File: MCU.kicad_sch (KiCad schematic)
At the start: 3 parts, among them J2 Micro_SD_Card, U3 STM32H503KBUx, U7 47L16

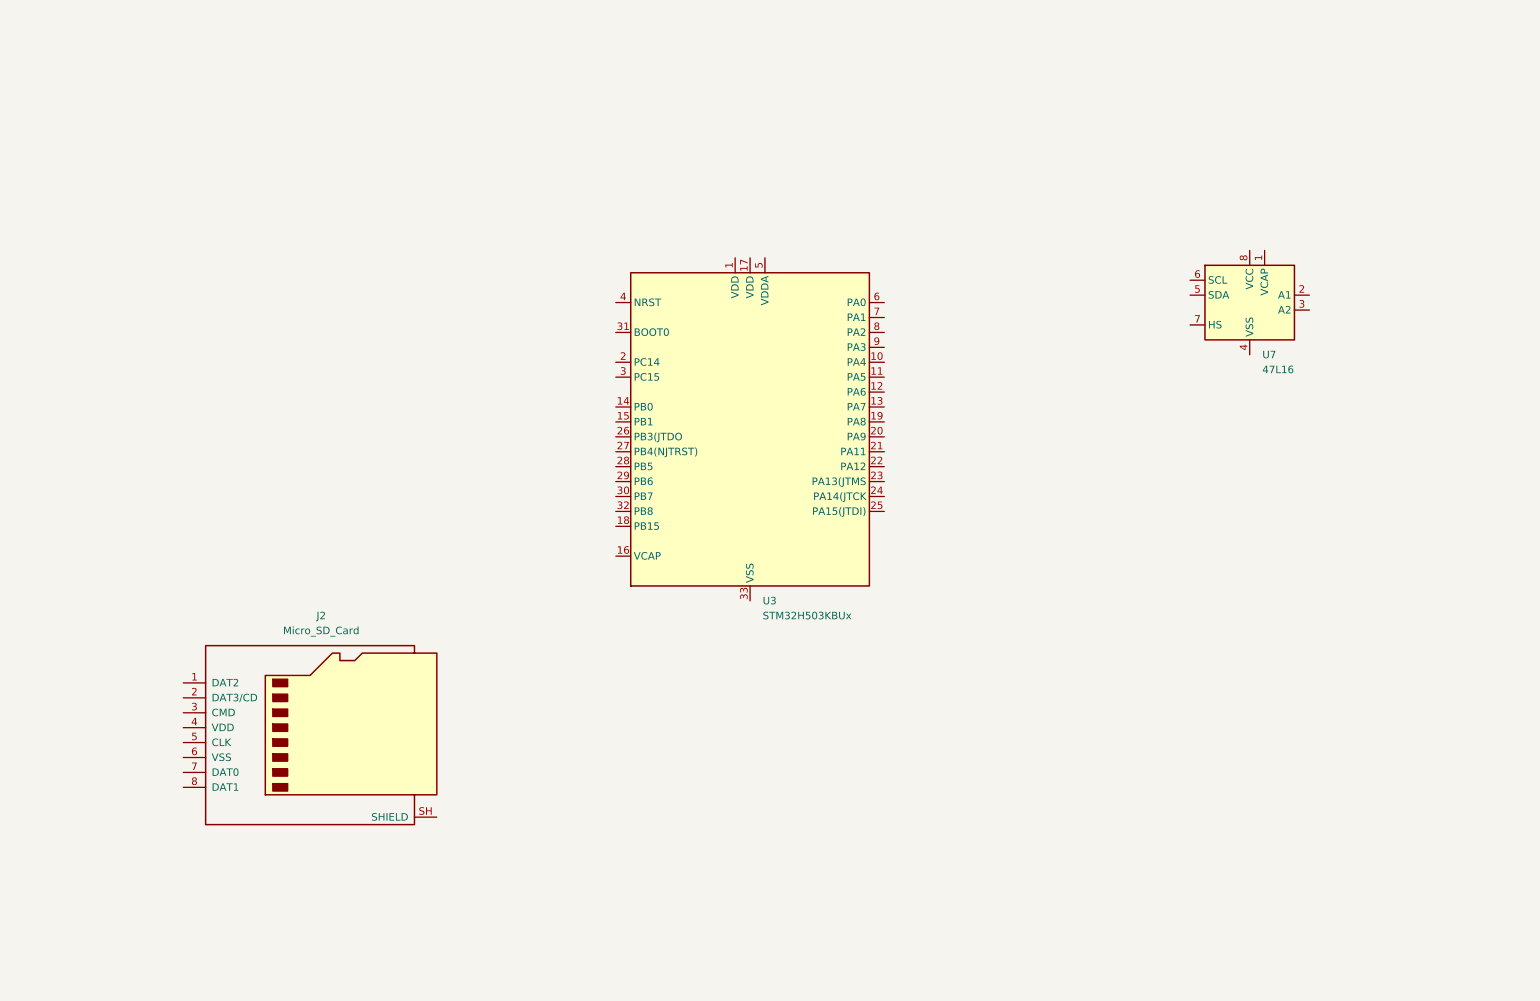
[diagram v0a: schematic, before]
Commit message: Added power schematic
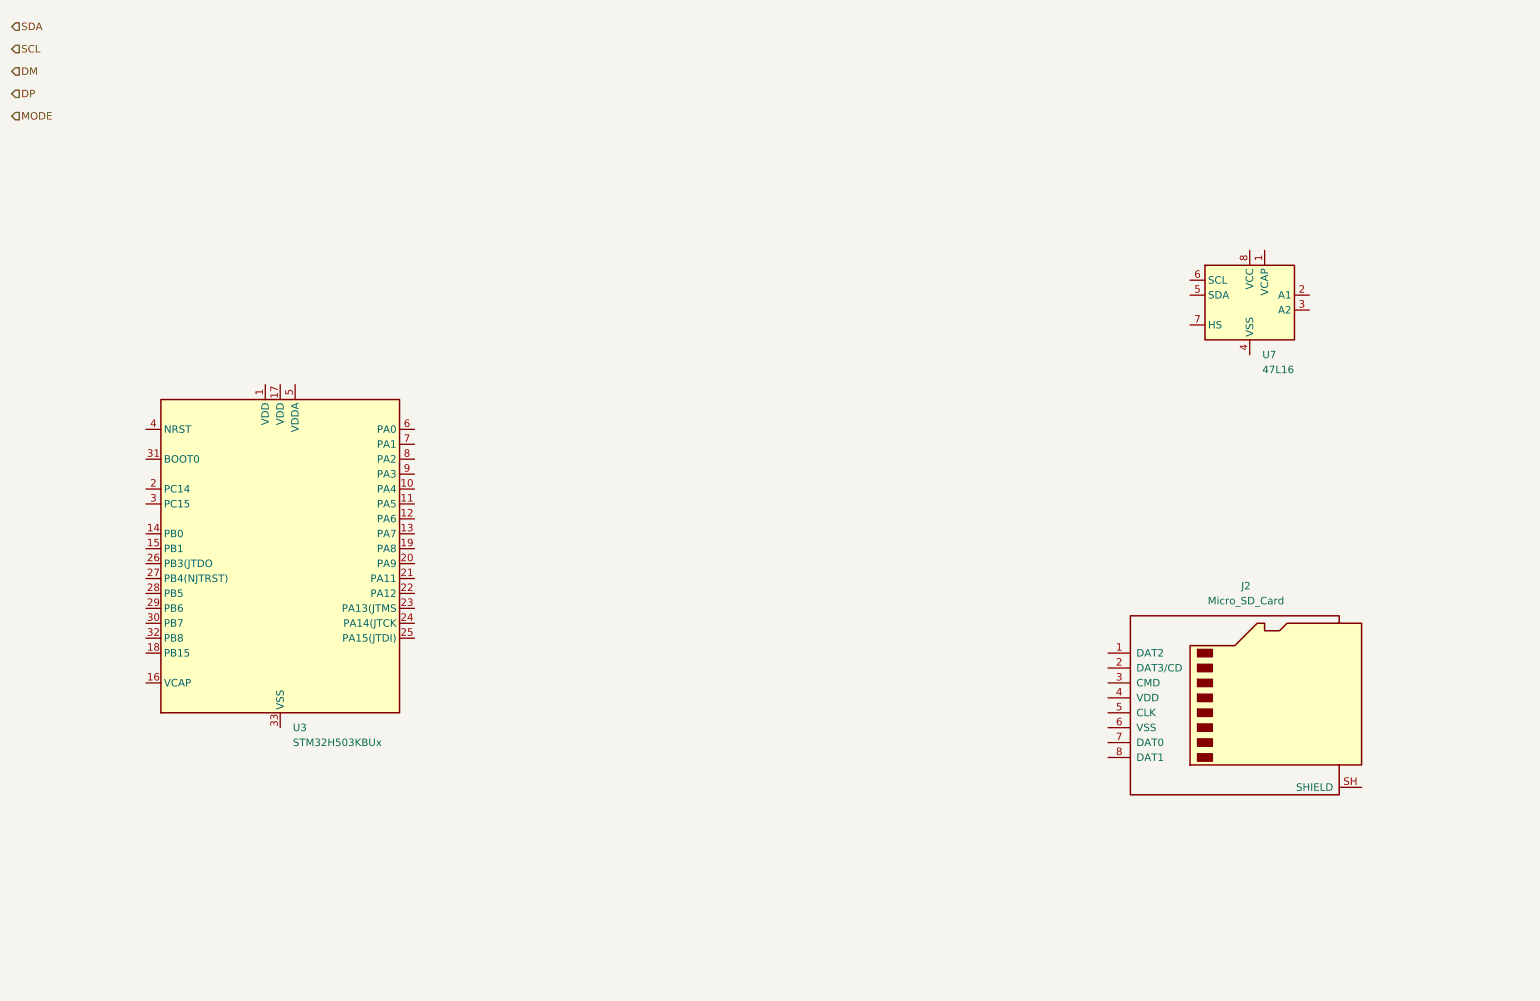
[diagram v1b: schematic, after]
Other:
- moved on the sheet: J2, U3

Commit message: Added todos
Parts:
- removed U3: STM32H503KBUx, Package_DFN_QFN:QFN-32-1EP_5x5mm_P0.5mm_EP3.45x3.45mm, symbol MCU_ST_STM32H5:STM32H503KBUx
- added C12, C13: 2u2, Capacitor_SMD:C_0603_1608Metric, symbol Device:C
- added J1: SWD, Connector_PinHeader_2.54mm:PinHeader_1x04_P2.54mm_Vertical, symbol Connector:Conn_01x04_Pin
- added SW2: SW_Push, symbol Switch:SW_Push
- added U3: STM32H503CBUx, Package_DFN_QFN:QFN-48-1EP_7x7mm_P0.5mm_EP5.6x5.6mm, symbol MCU_ST_STM32H5:STM32H503CBUx
- added U9: 32MHz, symbol diamond-symlib:ECS-TXO-2016
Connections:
- new net: C13.1, U3.22 (VCAP)
- new net: C12.1, U3.46 (VCAP)
- new net: U3.5 (PH0), U9.3 (OUT)
- new net +3V3: U3.1 (VBAT), U3.24 (VDD), U3.36 (VDD), U3.48 (VDD), U3.9 (VDDA), U9.1 (TRI), U9.4 (VDD)
- new net GND: C12.2, C13.2, U3.23 (VSS), U3.35 (VSS), U3.47 (VSS), U3.49 (VSS), U3.8 (VSSA)
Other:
- moved on the sheet: J2

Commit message: Started PCB
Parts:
- added C18: 22u, Capacitor_SMD:C_0805_2012Metric, symbol Device:C
- added C19, C20, C21: 1u, Capacitor_SMD:C_0603_1608Metric, symbol Device:C
- added C22, C23: 100n, Capacitor_SMD:C_0402_1005Metric, symbol Device:C
- added J4: Conn_01x21_Pin, Connector_PinSocket_2.54mm:PinSocket_1x21_P2.54mm_Vertical, symbol Connector:Conn_01x21_Pin
- added R18, R19, R20, R21, R22, R23: 4k7, Resistor_SMD:R_0603_1608Metric, symbol Device:R
- added SW3: SW_Push, symbol Switch:SW_Push
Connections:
- net +3V3: now also J2.4 (VDD), U7.8 (VCC), C19.1, C22.1, C23.1, R18.1, R19.1, R20.1, R21.1, R22.1, SW3.1
- net DM: now also U3.32 (PA11)
- net DP: now also U3.33 (PA12)
- net GND: now also J2.6 (VSS), J2.SH (SHIELD), SW2.1, U7.2 (A1), U7.3 (A2), U7.4 (VSS), U7.7 (HS), U9.2 (GND), C18.2, C19.2, C20.2, C21.2, C22.2, C23.2, R23.2
- net SCL: now also U7.6 (SCL), R20.2, R21.2
- net SDA: now also U7.5 (SDA), R18.2, R19.2
- net MISO: now reaches U3.10 (PA0)
- net MISO: now also J2.7 (DAT0)
- net CS: now reaches U3.11 (PA1)
- net CS: now also J2.2 (DAT3/CD)
- net SCLK: now reaches U3.12 (PA2)
- net SCLK: now also J2.5 (CLK)
- net MOSI: now reaches U3.14 (PA4)
- net MOSI: now also J2.3 (CMD)
- net CANRX: now reaches U3.25 (PB12)
- net CANTX: now reaches U3.26 (PB13)
- net SWDIO: now reaches U3.34 (PA13(JTMS)
- net SWCLK: now reaches U3.37 (PA14(JTCK)
- net SWO: now reaches U3.38 (PA15(JTDI))
- net BOOT0: now reaches U3.44 (BOOT0)
- net BOOT0: now also C21.1, R23.1, SW3.2
- net RST: now reaches U3.7 (NRST)
- net RST: now also SW2.2, C20.1, R22.2
- net at U7.1 (VCAP): now also C18.1
- no-connect marks 0 -> 6
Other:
- moved on the sheet: C12, C13, J1, J2, SW2, U3, U7, U9
